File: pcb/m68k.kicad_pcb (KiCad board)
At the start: 2 copper layers, 89 parts, among them J1 USB_B_Micro, J4 DB15_Male_HighDensity, U1 93LC56, U10 25LCxxx, U11 TXB0108DQSR, U12 TXB0108DQSR, U13 iCE40-HX4K-TQ144, U14 ADV7125KSTZ50, U15 74LVC1G17, U16 LD1117S33TR_SOT223, U17 LD1117S12TR_SOT223, U2 68000D, U3 FT2232H, U4 TXB0108DQSR, U5 TXB0108DQSR, U6 TXB0108DQSR, U7 SN74LVC8T245PWR, U8 SN74LVC8T245PWR, U9 AS6C1616, X1 ASV-12.000MHz

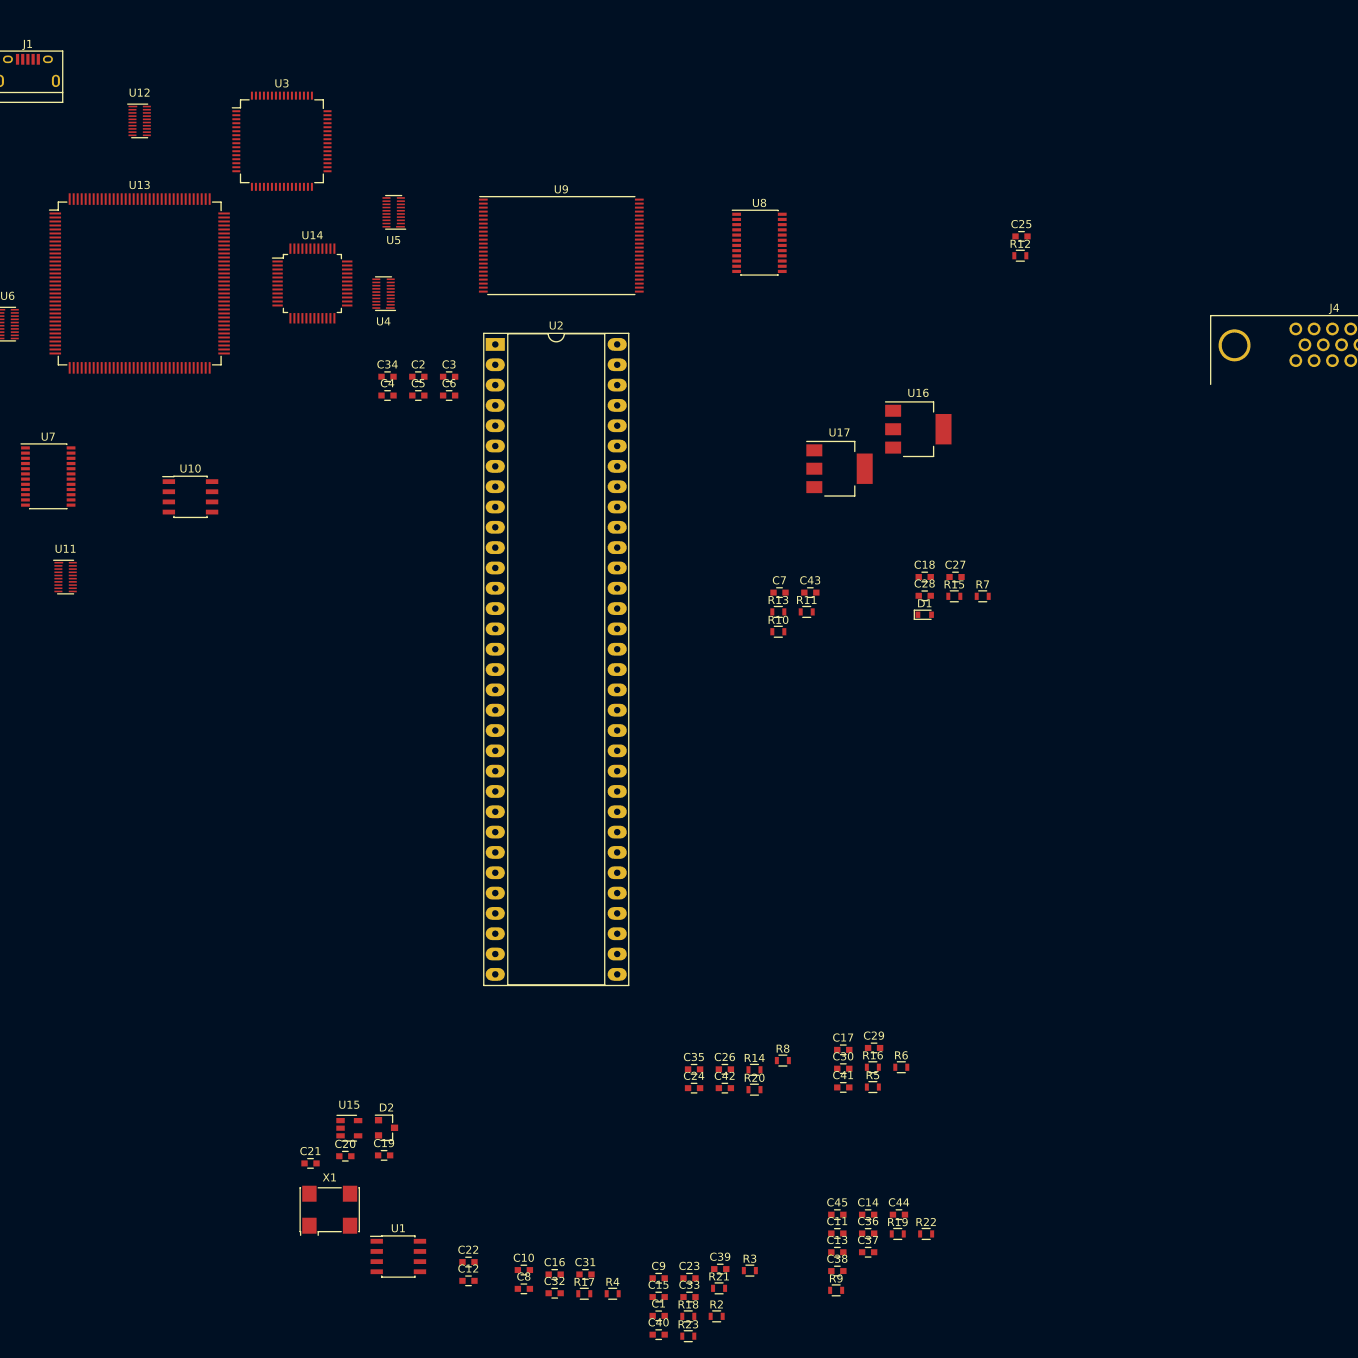
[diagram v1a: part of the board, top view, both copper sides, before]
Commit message: Update footprints (Mini DIN for PS/2 still missing)
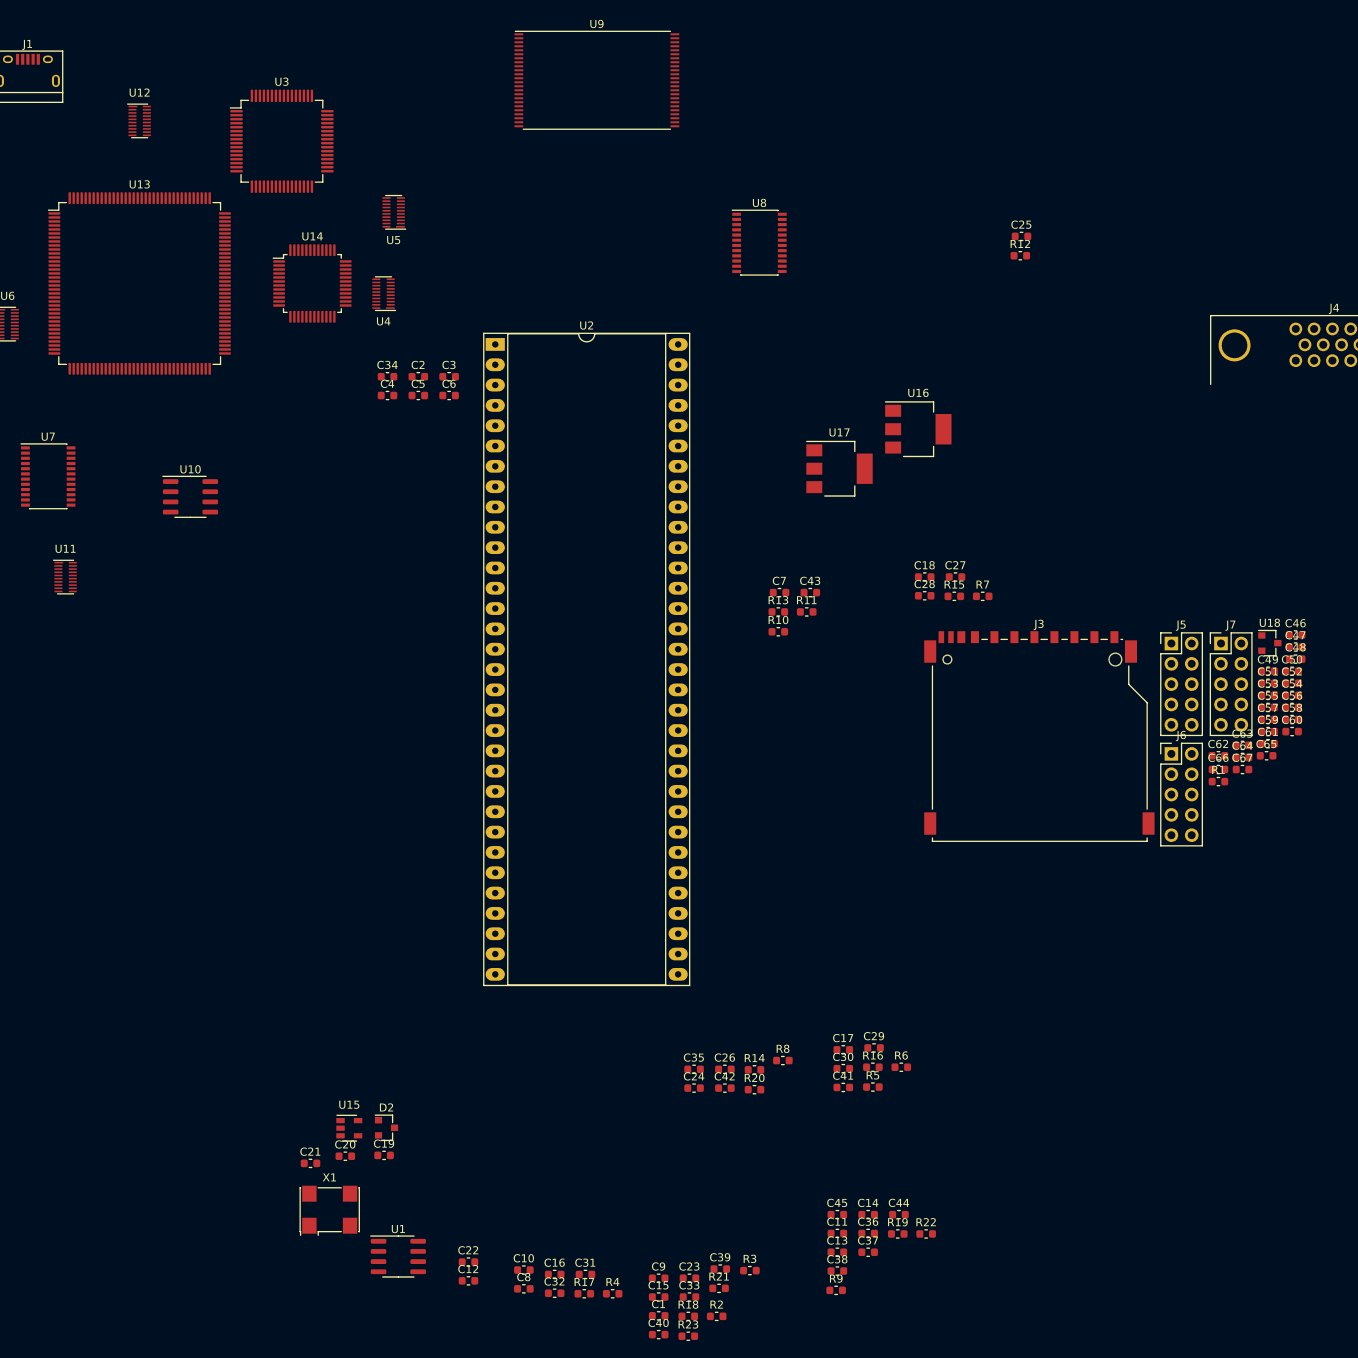
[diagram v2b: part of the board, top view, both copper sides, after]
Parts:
- removed D1: D_Schottky, Diodes_SMD:D_0603
- added C46: 0.01uF, Capacitor_SMD:C_0603_1608Metric, F.Cu at (215.6, 104.9)
- added C47: 0.01uF, Capacitor_SMD:C_0603_1608Metric, F.Cu at (215.6, 106.4)
- added C48: 0.01uF, Capacitor_SMD:C_0603_1608Metric, F.Cu at (215.6, 107.9)
- added C49: 0.01uF, Capacitor_SMD:C_0603_1608Metric, F.Cu at (212.2, 109.4)
- added C50: 0.01uF, Capacitor_SMD:C_0603_1608Metric, F.Cu at (215.2, 109.4)
- added C51: 0.01uF, Capacitor_SMD:C_0603_1608Metric, F.Cu at (212.2, 110.9)
- added C52: 0.01uF, Capacitor_SMD:C_0603_1608Metric, F.Cu at (215.2, 110.9)
- added C53: 0.01uF, Capacitor_SMD:C_0603_1608Metric, F.Cu at (212.2, 112.4)
- added C54: 0.01uF, Capacitor_SMD:C_0603_1608Metric, F.Cu at (215.2, 112.4)
- added C55: 0.01uF, Capacitor_SMD:C_0603_1608Metric, F.Cu at (212.2, 114.0)
- added C56: 0.01uF, Capacitor_SMD:C_0603_1608Metric, F.Cu at (215.2, 114.0)
- added C57: 0.01uF, Capacitor_SMD:C_0603_1608Metric, F.Cu at (212.2, 115.5)
- added C58: 0.01uF, Capacitor_SMD:C_0603_1608Metric, F.Cu at (215.2, 115.5)
- added C59: 0.01uF, Capacitor_SMD:C_0603_1608Metric, F.Cu at (212.2, 117.0)
- added C60: 0.01uF, Capacitor_SMD:C_0603_1608Metric, F.Cu at (215.2, 117.0)
- added C61: 0.01uF, Capacitor_SMD:C_0603_1608Metric, F.Cu at (212.2, 118.5)
- added C62: 0.01uF, Capacitor_SMD:C_0603_1608Metric, F.Cu at (206.0, 120.0)
- added C63: 0.01uF, Capacitor_SMD:C_0603_1608Metric, F.Cu at (209.0, 118.7)
- added C64: 0.01uF, Capacitor_SMD:C_0603_1608Metric, F.Cu at (209.0, 120.2)
- added C65: 0.01uF, Capacitor_SMD:C_0603_1608Metric, F.Cu at (212.0, 120.0)
- added C66: 0.01uF, Capacitor_SMD:C_0603_1608Metric, F.Cu at (206.0, 121.7)
- added C67: 0.01uF, Capacitor_SMD:C_0603_1608Metric, F.Cu at (209.0, 121.7)
- added J3: SD_Card, Connector_Card:SD_TE_2041021, F.Cu at (183.6, 117.1)
- added J5: FTSH-105-01-L-DV-K, Connector_PinHeader_2.54mm:PinHeader_2x05_P2.54mm_Vertical, F.Cu at (200.1, 106.0)
- added J6: FTSH-105-01-L-DV-K, Connector_PinHeader_2.54mm:PinHeader_2x05_P2.54mm_Vertical, F.Cu at (200.1, 119.8)
- added J7: FTSH-105-01-L-DV-K, Connector_PinHeader_2.54mm:PinHeader_2x05_P2.54mm_Vertical, F.Cu at (206.3, 106.0)
- added R1: 100, Resistor_SMD:R_0603_1608Metric, F.Cu at (206.0, 123.2)
- added U18: ATL431BQDBZR, Package_TO_SOT_SMD:SOT-23, F.Cu at (212.4, 105.9)
- C1, C10, C11, C12, C13, C14, C15, C16, C17, C18, C19, C2, C20, C21, C22, C23, C24, C25, C26, C27, C28, C29, C3, C30, C31, C32, C33, C34, C35, C36, C37, C38, C39, C4, C40, C41, C42, C43, C44, C45, C5, C6, C7, C8, C9: footprint Capacitors_SMD:C_0603 -> Capacitor_SMD:C_0603_1608Metric
- D2: footprint TO_SOT_Packages_SMD:SOT-23 -> Package_TO_SOT_SMD:SOT-23
- J4: footprint Connectors_DSub:DSUB-15-HD_Female_Horizontal_Pitch2.29x1.98mm_EdgePinOffset3.03mm_Housed_MountingHolesOffset4.94mm -> Connector_Dsub:DSUB-15-HD_Female_Horizontal_P2.29x1.98mm_EdgePinOffset3.03mm_Housed_MountingHolesOffset4.94mm
- R10, R11, R12, R13, R14, R15, R16, R17, R18, R19, R2, R20, R21, R22, R23, R3, R4, R5, R6, R7, R8, R9: footprint Resistors_SMD:R_0603 -> Resistor_SMD:R_0603_1608Metric
- U1, U10: footprint Housings_SOIC:SOIC-8_3.9x4.9mm_Pitch1.27mm -> Package_SO:SOIC-8_3.9x4.9mm_P1.27mm
- U11, U12, U4, U5, U6: footprint Housings_SON:USON-20_2x4mm_Pitch0.4mm -> Package_SON:USON-20_2x4mm_P0.4mm
- U13: footprint Housings_QFP:TQFP-144_20x20mm_Pitch0.5mm -> Package_QFP:TQFP-144_20x20mm_P0.5mm
- U14: footprint Housings_QFP:LQFP-48_7x7mm_Pitch0.5mm -> Package_QFP:LQFP-48_7x7mm_P0.5mm
- U15: footprint TO_SOT_Packages_SMD:SOT-23-5 -> Package_TO_SOT_SMD:SOT-23-5
- U16, U17: footprint TO_SOT_Packages_SMD:SOT-223-3_TabPin2 -> Package_TO_SOT_SMD:SOT-223-3_TabPin2
- U2: footprint Housings_DIP:DIP-64_W15.24mm_Socket_LongPads -> Package_DIP:DIP-64_W22.86mm_Socket_LongPads
- U3: footprint Housings_QFP:LQFP-64_10x10mm_Pitch0.5mm -> Package_QFP:LQFP-64_10x10mm_P0.5mm
- U7, U8: footprint Housings_SSOP:TSSOP-24_4.4x7.8mm_Pitch0.65mm -> Package_SO:TSSOP-24_4.4x7.8mm_P0.65mm
- U9: footprint Housings_SSOP:TSOP-I-48_18.4x12mm_Pitch0.5mm -> Package_SO:TSOP-I-48_18.4x12mm_P0.5mm
- X1: footprint Oscillators:Oscillator_SMD_Abracon_ASV-4pin_7.0x5.1mm -> Oscillator:Oscillator_SMD_Abracon_ASV-4Pin_7.0x5.1mm
- moved U9 21.1 mm to (128.3, 35.6)
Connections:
- J1 pad 4: Net-(J1-Pad4) -> (no net)
- J4 pad 11: Net-(J4-Pad11) -> (no net)
- J4 pad 12: Net-(J4-Pad12) -> (no net)
- J4 pad 15: Net-(J4-Pad15) -> (no net)
- J4 pad 4: Net-(J4-Pad4) -> (no net)
- J4 pad 6: Net-(J4-Pad6) -> (no net)
- J4 pad 7: Net-(J4-Pad7) -> (no net)
- J4 pad 8: Net-(J4-Pad8) -> (no net)
- U1 pad 7: Net-(U1-Pad7) -> (no net)
- U11 pad 10: Net-(U11-Pad10) -> (no net)
- U11 pad 12: HALTn -> (no net)
- U11 pad 13: E -> (no net)
- U11 pad 14: VMAn -> FC2
- U11 pad 15: BGn -> FC1
- U11 pad 16: ASn -> FC0
- U11 pad 6: +3V3 -> ADDR_OE
- U11 pad 9: Net-(U11-Pad9) -> (no net)
- U12 pad 14: Net-(U12-Pad14) -> RESETn
- U12 pad 15: Net-(U12-Pad15) -> HALTn
- U12 pad 16: RESETn -> ASn
- U12 pad 17: FC2 -> E
- U12 pad 18: FC1 -> VMAn
- U12 pad 20: FC0 -> BGn
- U12 pad 4: CDONE -> Net-(U12-Pad4)
- U12 pad 8: Net-(U12-Pad8) -> CDONE
- U13 pad 109: Net-(U13-Pad109) -> (no net)
- U13 pad 133: Net-(U13-Pad133) -> (no net)
- U13 pad 138: Net-(U11-Pad9) -> Net-(U12-Pad1)
- U13 pad 139: Net-(U11-Pad10) -> Net-(U12-Pad2)
- U13 pad 141: Net-(U12-Pad1) -> Net-(U12-Pad3)
- U13 pad 142: Net-(U12-Pad2) -> Net-(U12-Pad4)
- U13 pad 143: Net-(U12-Pad3) -> Net-(U12-Pad7)
- U13 pad 24: Net-(U13-Pad24) -> BERRn
- U13 pad 25: Net-(U13-Pad25) -> (no net)
- U13 pad 35: Net-(U13-Pad35) -> (no net)
- U13 pad 36: Net-(U13-Pad36) -> (no net)
- U13 pad 50: Net-(U13-Pad50) -> (no net)
- U13 pad 51: Net-(U13-Pad51) -> (no net)
- U13 pad 58: Net-(U13-Pad58) -> (no net)
- U13 pad 77: Net-(U13-Pad77) -> (no net)
- U2 pad 22: +5V -> BERRn
- U3 pad 19: Net-(U3-Pad19) -> (no net)
- U3 pad 22: Net-(U3-Pad22) -> (no net)
- U3 pad 26: Net-(U3-Pad26) -> (no net)
- U3 pad 27: Net-(U3-Pad27) -> (no net)
- U3 pad 28: Net-(U3-Pad28) -> (no net)
- U3 pad 29: Net-(U3-Pad29) -> (no net)
- U3 pad 3: Net-(U3-Pad3) -> (no net)
- U3 pad 30: Net-(U3-Pad30) -> (no net)
- U3 pad 32: Net-(U3-Pad32) -> (no net)
- U3 pad 33: Net-(U3-Pad33) -> (no net)
- U3 pad 34: Net-(U3-Pad34) -> (no net)
- U3 pad 36: Net-(U3-Pad36) -> (no net)
- U3 pad 40: Net-(U3-Pad40) -> (no net)
- U3 pad 41: Net-(U3-Pad41) -> (no net)
- U3 pad 43: Net-(U3-Pad43) -> (no net)
- U3 pad 44: Net-(U3-Pad44) -> (no net)
- U3 pad 45: Net-(U3-Pad45) -> (no net)
- U3 pad 46: Net-(U3-Pad46) -> (no net)
- U3 pad 48: Net-(U3-Pad48) -> (no net)
- U3 pad 52: Net-(U3-Pad52) -> (no net)
- U3 pad 53: Net-(U3-Pad53) -> (no net)
- U3 pad 54: Net-(U3-Pad54) -> (no net)
- U3 pad 55: Net-(U3-Pad55) -> (no net)
- U3 pad 57: Net-(U3-Pad57) -> (no net)
- U3 pad 58: Net-(U3-Pad58) -> (no net)
- U3 pad 59: Net-(U3-Pad59) -> (no net)
- U3 pad 60: Net-(U3-Pad60) -> (no net)
- U6 pad 10: Net-(U6-Pad10) -> (no net)
- U6 pad 12: Net-(U6-Pad12) -> (no net)
- U7 pad 10: /d7 -> /d4
- U7 pad 14: /D7 -> /D4
- U7 pad 15: /D6 -> /D12
- U7 pad 17: /D4 -> /D13
- U7 pad 18: /D3 -> /D6
- U7 pad 19: /D2 -> /D14
- U7 pad 20: /D1 -> /D7
- U7 pad 21: /D0 -> /D15
- U7 pad 3: /d0 -> /d15
- U7 pad 4: /d1 -> /d7
- U7 pad 5: /d2 -> /d14
- U7 pad 6: /d3 -> /d6
- U7 pad 7: /d4 -> /d13
- U7 pad 9: /d6 -> /d12
- U8 pad 10: /d8 -> /d0
- U8 pad 14: /D8 -> /D0
- U8 pad 15: /D9 -> /D8
- U8 pad 16: /D10 -> /D1
- U8 pad 17: /D11 -> /D9
- U8 pad 18: /D12 -> /D2
- U8 pad 19: /D13 -> /D10
- U8 pad 20: /D14 -> /D3
- U8 pad 21: /D15 -> /D11
- U8 pad 3: /d15 -> /d11
- U8 pad 4: /d14 -> /d3
- U8 pad 5: /d13 -> /d10
- U8 pad 6: /d12 -> /d2
- U8 pad 7: /d11 -> /d9
- U8 pad 8: /d10 -> /d1
- U8 pad 9: /d9 -> /d8
- U9 pad 10: Net-(U9-Pad10) -> (no net)
- U9 pad 13: Net-(U9-Pad13) -> (no net)
- U9 pad 47: Net-(U9-Pad47) -> (no net)

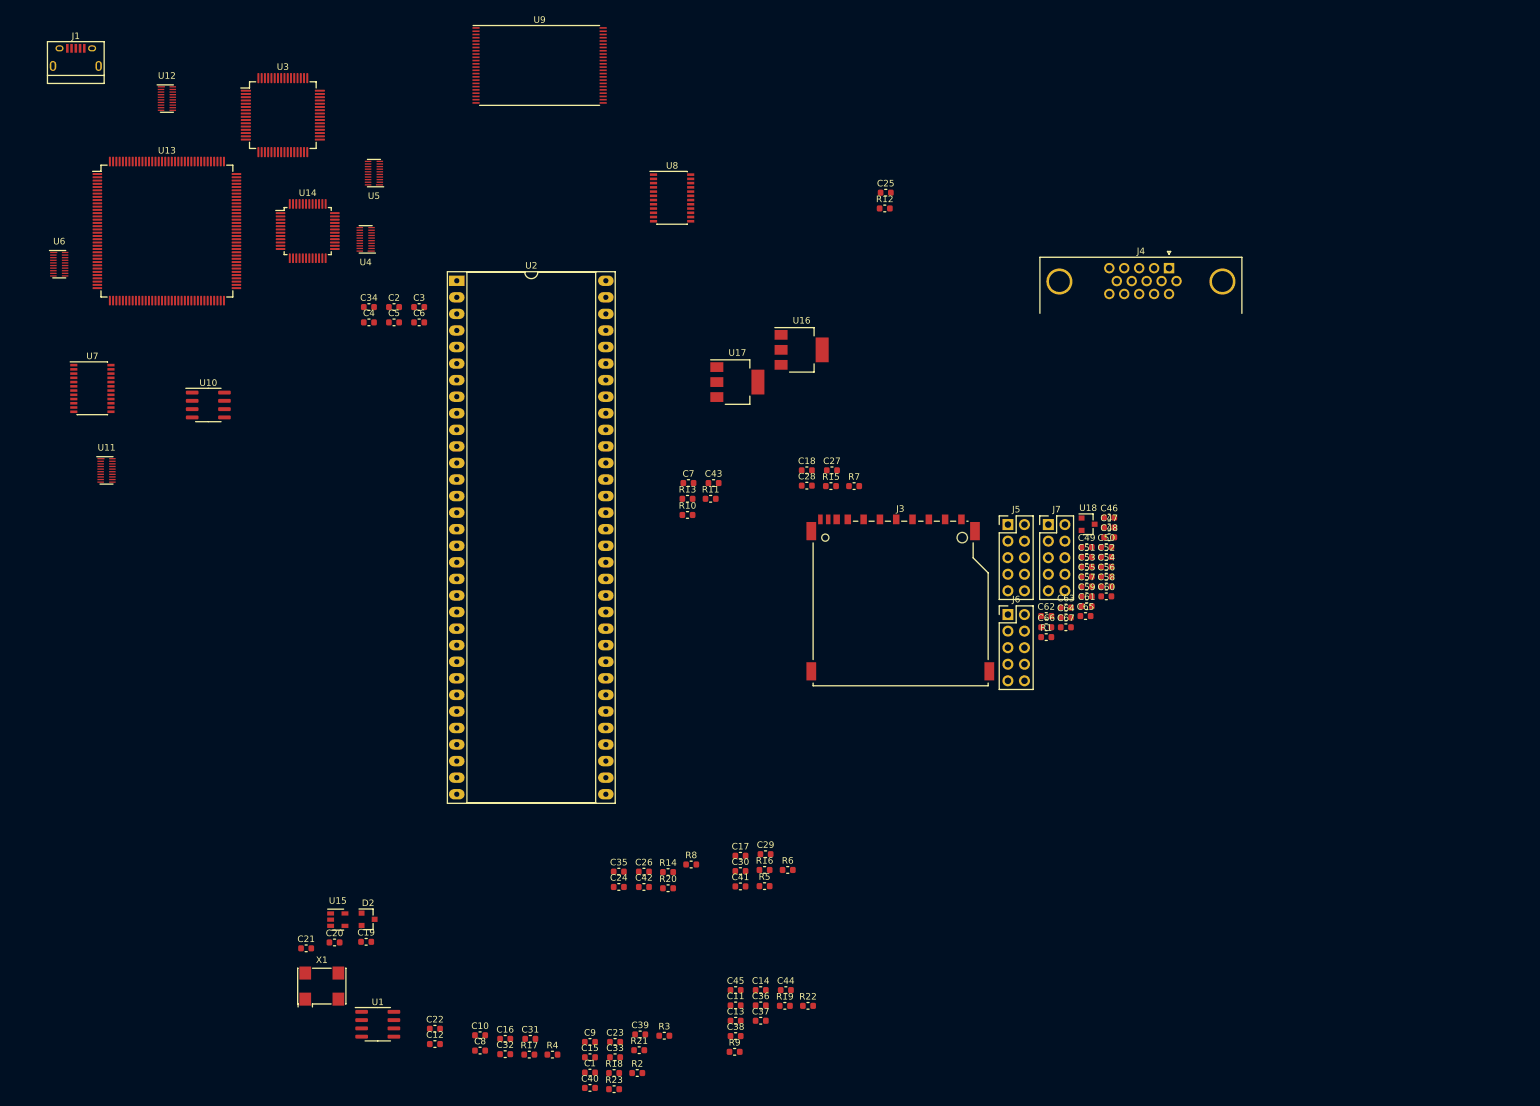
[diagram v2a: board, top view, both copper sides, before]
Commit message: start pcb layout
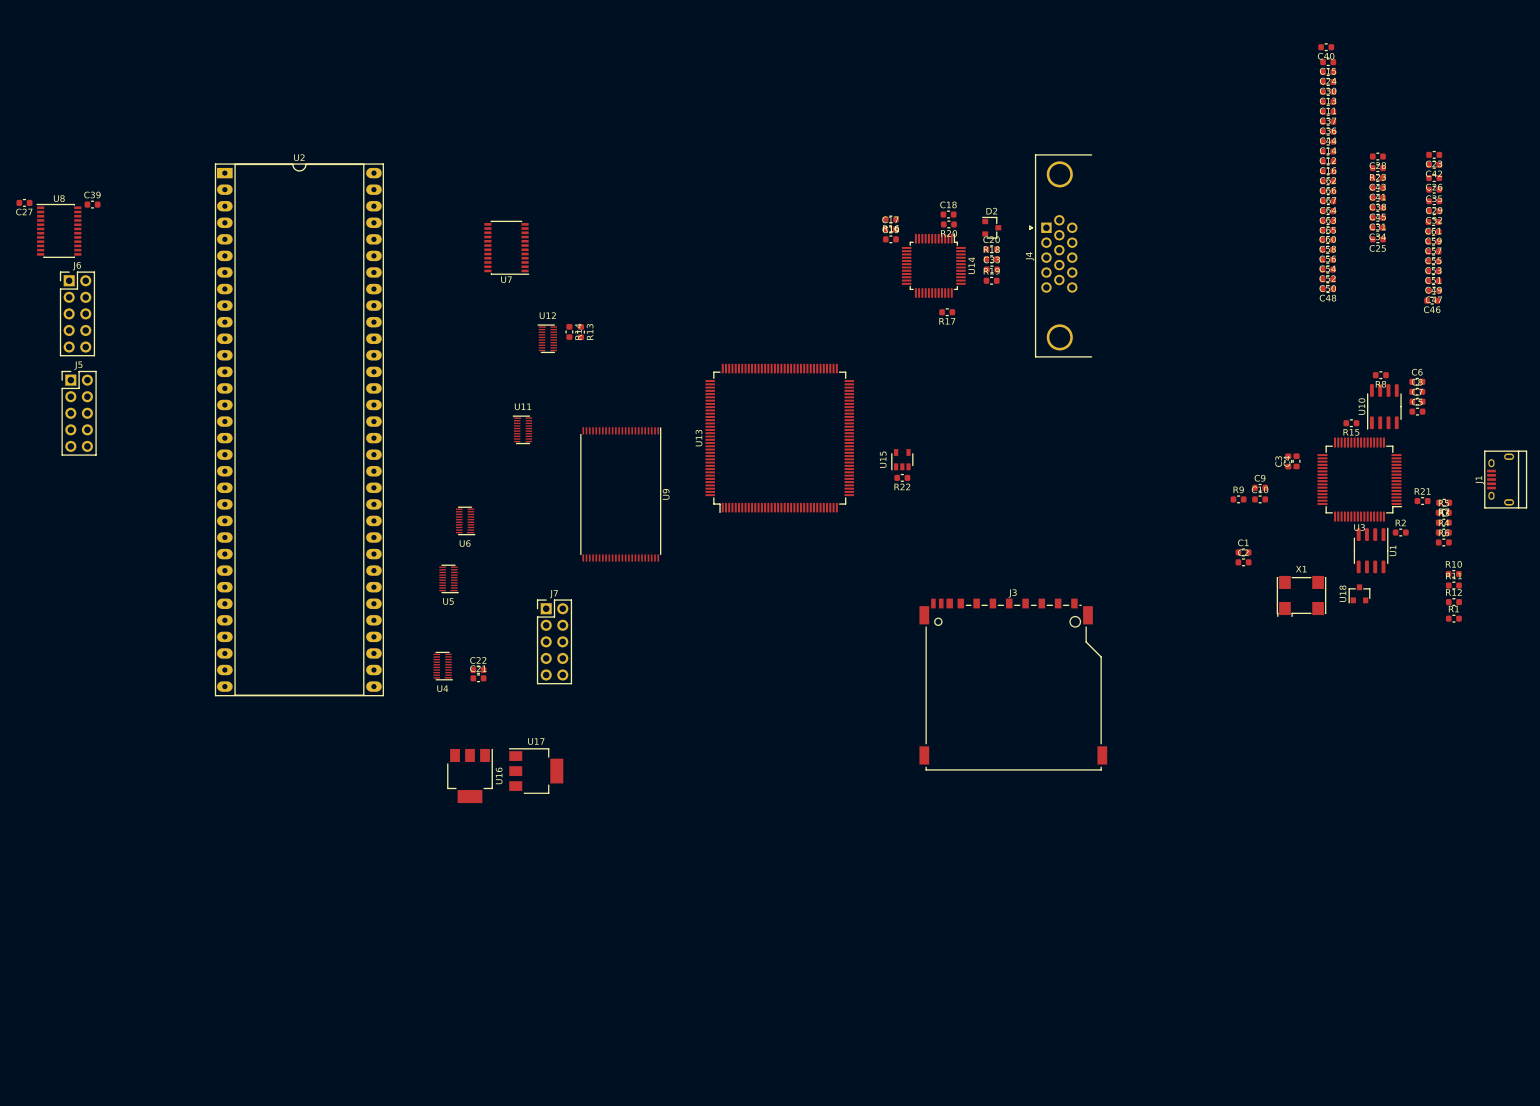
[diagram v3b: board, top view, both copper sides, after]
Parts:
- moved J1 227.8 mm to (275.6, 99.1), turned to 90 degrees
- moved C40 195.5 mm to (248.9, 32.8), turned to 180 degrees
- moved C12 193.6 mm to (249.2, 48.8), turned to 180 degrees
- moved C32 192.4 mm to (265.5, 57.9), turned to 180 degrees
- moved C15 190.0 mm to (249.2, 35.1), turned to 180 degrees
- moved C23 185.2 mm to (265.5, 49.3), turned to 180 degrees
- moved C16 184.5 mm to (249.2, 50.3), turned to 180 degrees
- moved R23 183.5 mm to (256.8, 51.3), turned to 180 degrees
- moved C31 181.0 mm to (256.8, 58.9), turned to 180 degrees
- moved U10 180.3 mm to (257.8, 87.9), turned to 90 degrees
- moved C8 175.7 mm to (262.9, 85.6)
- moved U3 174.3 mm to (254.0, 99.1), turned to 180 degrees
- moved C13 168.9 mm to (249.2, 39.6), turned to 180 degrees
- moved U1 168.7 mm to (255.8, 110.0), turned to 270 degrees
- moved C11 165.7 mm to (249.2, 41.1), turned to 180 degrees
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
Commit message: update io
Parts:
- moved C15 153.3 mm to (118.1, 114.6), turned to 0 degrees
- moved C23 146.4 mm to (120.4, 69.3), turned to 270 degrees
- moved C27 115.5 mm to (146.5, 118.9)
- moved C39 110.2 mm to (146.6, 124.7), turned to 180 degrees
- moved U8 105.4 mm to (140.7, 121.7), turned to 270 degrees
- moved C40 0.79 mm to (249.2, 33.5), turned to 270 degrees
